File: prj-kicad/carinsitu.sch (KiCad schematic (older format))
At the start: 44 parts, among them P1 BAT, P2 MOT, P3 CONN_3, P4 CONN_1, SW1 SWITCH_SLIDE, U1 ESP8285, U2 MIC2860, U3 MAX17205, U4 SN74LVC1T45, U7 LSM6D3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

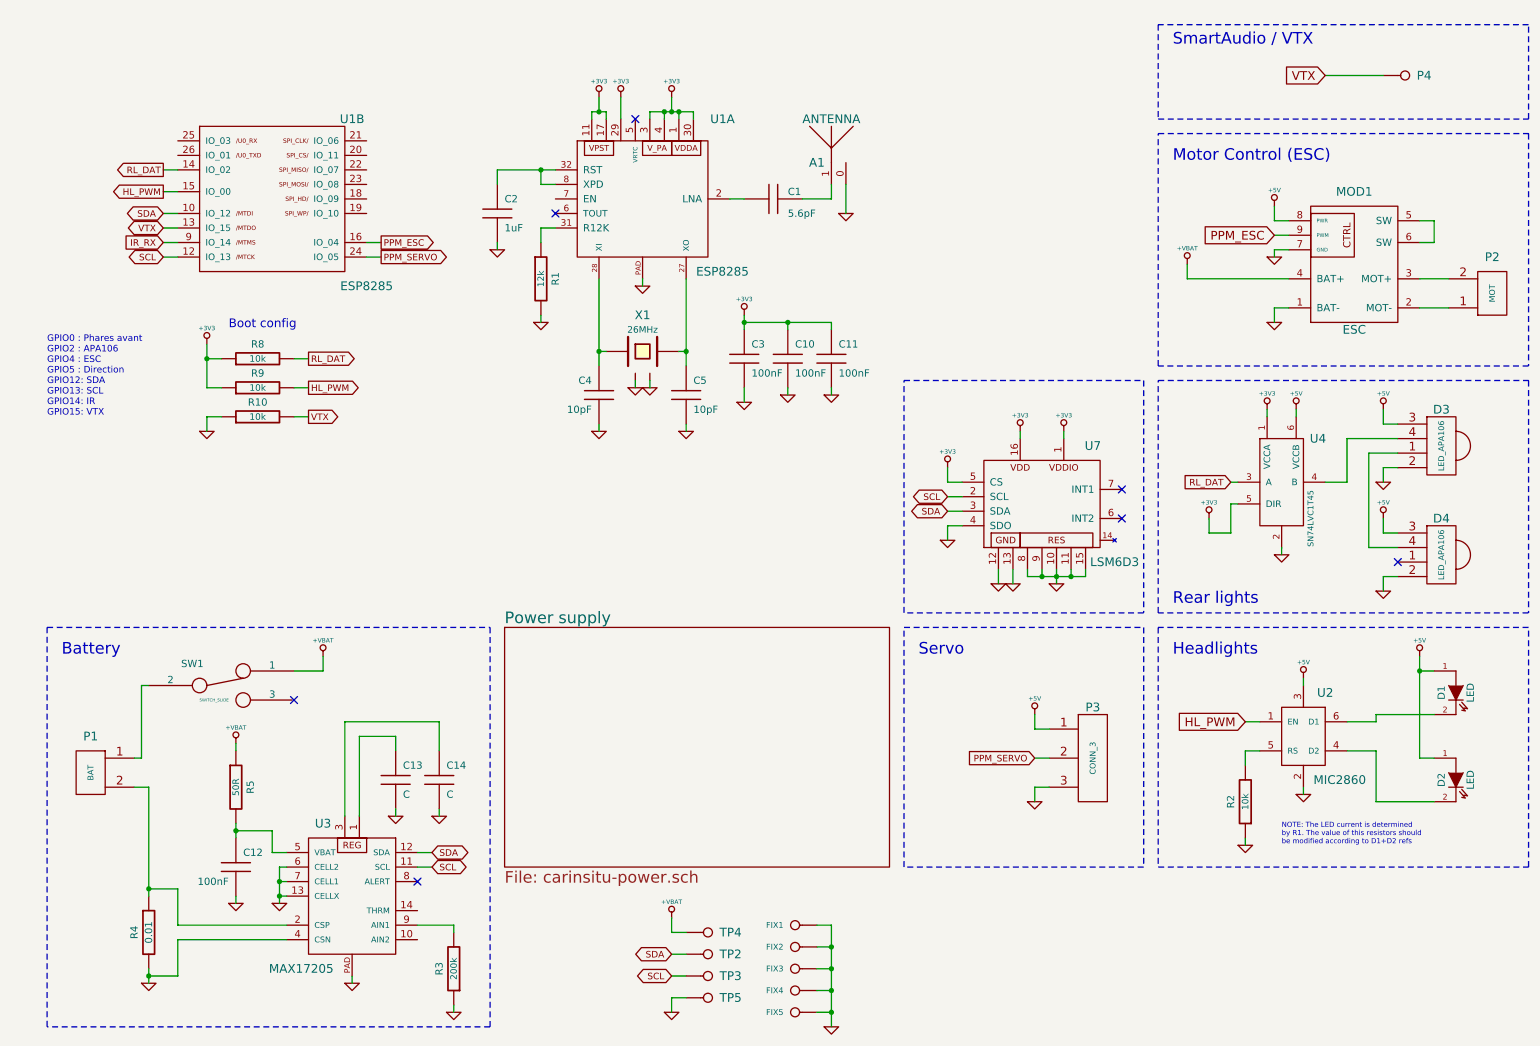
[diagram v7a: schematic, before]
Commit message: = UPD: Improve power (add decoupling caps), Add test-points for main signals, Add a level shifter for servo
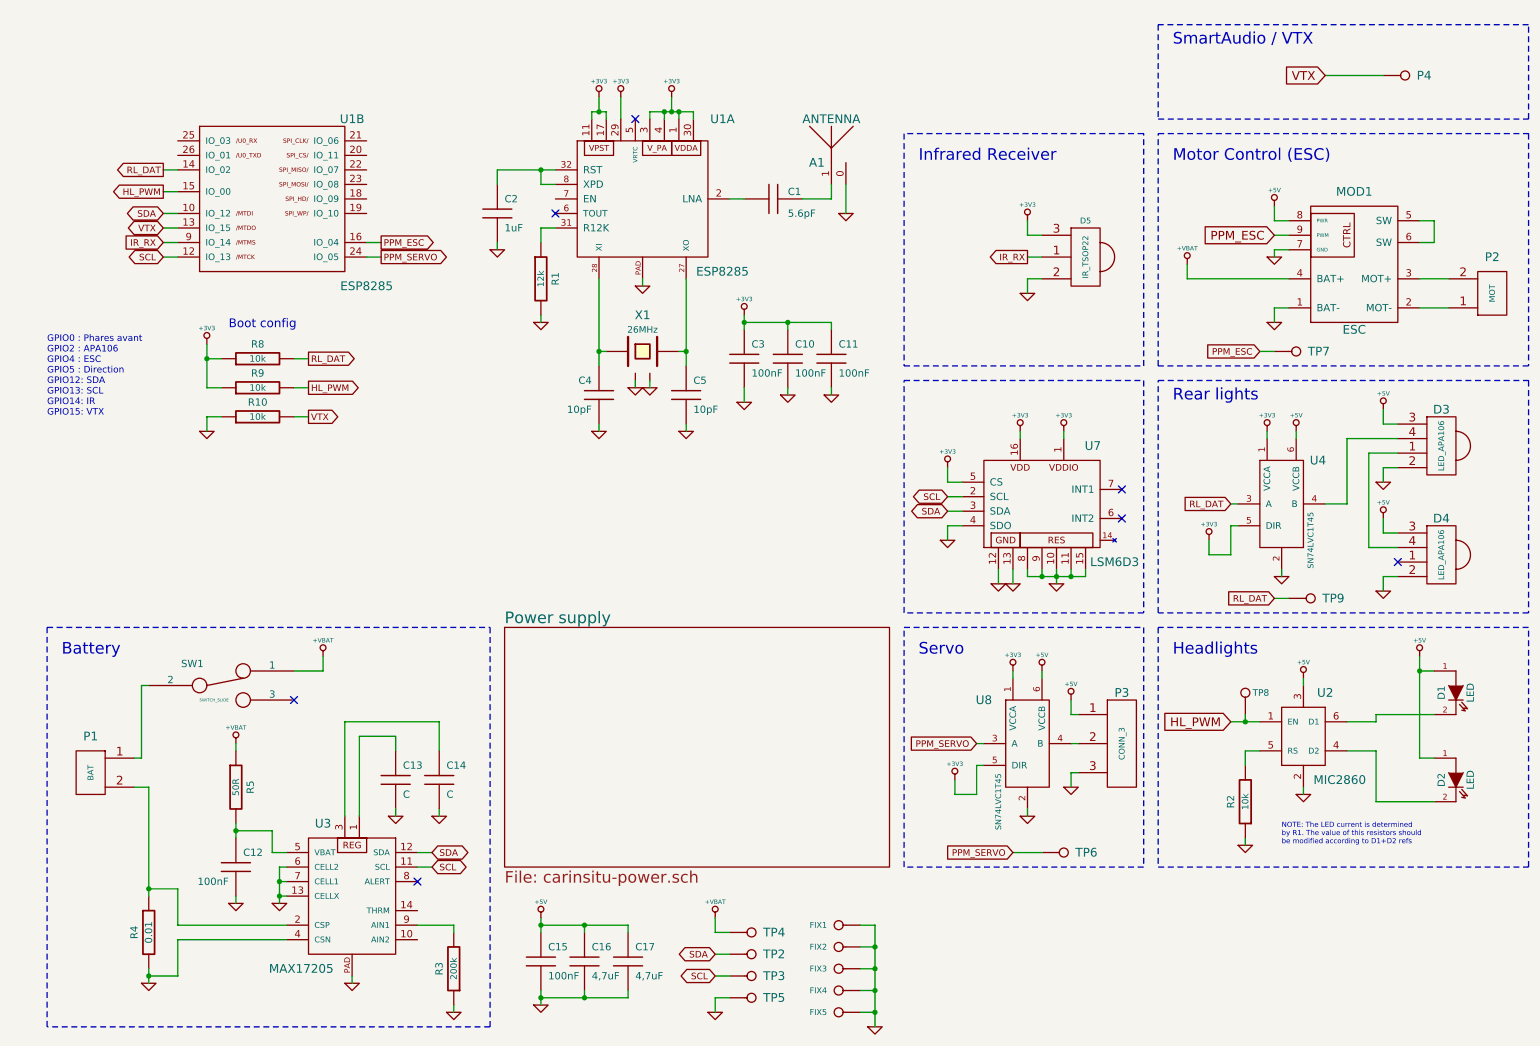
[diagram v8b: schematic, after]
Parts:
- added C15: 100nF, carinsitu:SMD0603, symbol C
- added C16, C17: 4,7uF, carinsitu:SMD0805, symbol C
- added D5: IR_TSOP22, carinsitu:CONN_61300311121, symbol IR_TSOP22
- added TP6, TP7, TP8, TP9: CONN_1, carinsitu:TP, symbol CONN_1
- added U8: SN74LVC1T45, carinsitu:SOT23-6, symbol SN74LVC1T45
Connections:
- net +3V3: now also D5.3 (VDD), U8.1 (VCCA), U8.5 (DIR)
- net +5V: now also C15.1, C16.1, C17.1, U8.6 (VCCB)
- net GND: now also C15.2, C16.2, C17.2, D5.2 (GND), U8.2
- net HL_PWM: now also TP8.1
- net IR_RX: now also D5.1 (DOUT)
- net PPM_ESC: now also TP7.1
- net PPM_SERVO: now also TP6.1, U8.3 (A); no longer P3.2 (P2)
- net RL_DAT: now also TP9.1
- new net: P3.2 (P2), U8.4 (B)
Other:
- note added: "Infrared Receiver"
- moved on the sheet: FIX1, FIX2, FIX3, FIX4, FIX5, P3, TP2, TP3, TP4, TP5, U4
